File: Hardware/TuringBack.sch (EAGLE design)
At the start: 43 parts, among them IC11 78L09, IC12 78L09, IC7 TL072P

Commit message: Rev 4 Front and Back Boards complete
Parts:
- renumbered BACK_BUS2 to LINK1, BACK_PWR to LINK2, BUS_1_BACK to LINK3
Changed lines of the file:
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@@
 <part name="L1" library="inductors" deviceset="BL0" device="1RN1A"/>
 <part name="L2" library="inductors" deviceset="BL0" device="1RN1A"/>
-<part name="BACK_PWR" library="con-lstb" deviceset="MA03-2" device=""/>
+<part name="LINK2" library="con-lstb" deviceset="MA03-2" device=""/>
 <part name="R4" library="TomW" deviceset="R-EU_" device="0207/7" value="100k"/>
 <part name="C19" library="TomW" deviceset="C-EU" device="050-024X044" value="100n"/>
@@
 <part name="C24" library="TomW" deviceset="C-EU" device="050-024X044" value="100n"/>
 <part name="C25" library="TomW" deviceset="C-EU" device="050-024X044" value="100n"/>
-<part name="BACK_BUS2" library="con-lstb" deviceset="MA03-2" device=""/>
-<part name="BUS_1_BACK" library="con-lstb" deviceset="MA05-2" device=""/>
+<part name="LINK1" library="con-lstb" deviceset="MA03-2" device=""/>
+<part name="LINK3" library="con-lstb" deviceset="MA05-2" device=""/>
 </parts>
 <sheets>
@@
 <instance part="GATES" gate="G$1" x="43.18" y="50.8"/>
 <instance part="PULSES" gate="G$1" x="93.98" y="50.8"/>
-<instance part="BACK_PWR" gate="1" x="157.48" y="35.56"/>
-<instance part="BACK_BUS2" gate="1" x="157.48" y="20.32"/>
-<instance part="BUS_1_BACK" gate="G$1" x="157.48" y="53.34"/>
+<instance part="LINK2" gate="1" x="157.48" y="35.56"/>
+<instance part="LINK1" gate="1" x="157.48" y="20.32"/>
+<instance part="LINK3" gate="G$1" x="157.48" y="53.34"/>
 <instance part="AND_2" gate="C" x="215.9" y="109.22"/>
 <instance part="AND_2" gate="D" x="218.44" y="86.36"/>
@@
 </segment>
 <segment>
-<pinref part="BACK_BUS2" gate="1" pin="5"/>
+<pinref part="LINK1" gate="1" pin="5"/>
 <wire x1="167.64" y1="22.86" x2="165.1" y2="22.86" width="0.1524" layer="91"/>
 <label x="167.64" y="22.86" size="1.016" layer="95" xref="yes"/>
@@
 </segment>
 <segment>
-<pinref part="BACK_BUS2" gate="1" pin="6"/>
+<pinref part="LINK1" gate="1" pin="6"/>
 <wire x1="147.32" y1="22.86" x2="149.86" y2="22.86" width="0.1524" layer="91"/>
 <label x="147.32" y="22.86" size="1.016" layer="95" rot="R180" xref="yes"/>
@@
 </segment>
 <segment>
-<pinref part="BACK_PWR" gate="1" pin="6"/>
+<pinref part="LINK2" gate="1" pin="6"/>
 <wire x1="147.32" y1="38.1" x2="149.86" y2="38.1" width="0.1524" layer="91"/>
 <label x="147.32" y="38.1" size="1.016" layer="95" rot="R180" xref="yes"/>
 </segment>
 <segment>
-<pinref part="BACK_PWR" gate="1" pin="5"/>
+<pinref part="LINK2" gate="1" pin="5"/>
 <wire x1="167.64" y1="38.1" x2="165.1" y2="38.1" width="0.1524" layer="91"/>
 <label x="167.64" y="38.1" size="1.016" layer="95" xref="yes"/>
@@
 </segment>
 <segment>
-<pinref part="BACK_PWR" gate="1" pin="4"/>
+<pinref part="LINK2" gate="1" pin="4"/>
 <wire x1="147.32" y1="35.56" x2="149.86" y2="35.56" width="0.1524" layer="91"/>
 <label x="147.32" y="35.56" size="1.016" layer="95" rot="R180" xref="yes"/>
 </segment>
 <segment>
-<pinref part="BACK_PWR" gate="1" pin="3"/>
+<pinref part="LINK2" gate="1" pin="3"/>
 <wire x1="167.64" y1="35.56" x2="165.1" y2="35.56" width="0.1524" layer="91"/>
 <label x="167.64" y="35.56" size="1.016" layer="95" xref="yes"/>
@@
 </segment>
 <segment>
-<pinref part="BACK_BUS2" gate="1" pin="4"/>
+<pinref part="LINK1" gate="1" pin="4"/>
 <wire x1="147.32" y1="20.32" x2="149.86" y2="20.32" width="0.1524" layer="91"/>
 <label x="147.32" y="20.32" size="1.016" layer="95" rot="R180" xref="yes"/>
@@
 <wire x1="167.64" y1="58.42" x2="165.1" y2="58.42" width="0.1524" layer="91"/>
 <label x="167.64" y="58.42" size="1.016" layer="95" xref="yes"/>
-<pinref part="BUS_1_BACK" gate="G$1" pin="9"/>
+<pinref part="LINK3" gate="G$1" pin="9"/>
 </segment>
 <segment>
@@
 </segment>
 <segment>
-<pinref part="BACK_BUS2" gate="1" pin="2"/>
+<pinref part="LINK1" gate="1" pin="2"/>
 <wire x1="147.32" y1="17.78" x2="149.86" y2="17.78" width="0.1524" layer="91"/>
 <label x="147.32" y="17.78" size="1.016" layer="95" rot="R180" xref="yes"/>
@@
 </segment>
 <segment>
-<pinref part="BACK_BUS2" gate="1" pin="3"/>
+<pinref part="LINK1" gate="1" pin="3"/>
 <wire x1="167.64" y1="20.32" x2="165.1" y2="20.32" width="0.1524" layer="91"/>
 <label x="167.64" y="20.32" size="1.016" layer="95" xref="yes"/>
@@
 <wire x1="167.64" y1="48.26" x2="165.1" y2="48.26" width="0.1524" layer="91"/>
 <label x="167.64" y="48.26" size="1.016" layer="95" xref="yes"/>
-<pinref part="BUS_1_BACK" gate="G$1" pin="1"/>
+<pinref part="LINK3" gate="G$1" pin="1"/>
 </segment>
 <segment>
@@
 <wire x1="147.32" y1="48.26" x2="149.86" y2="48.26" width="0.1524" layer="91"/>
 <label x="147.32" y="48.26" size="1.016" layer="95" rot="R180" xref="yes"/>
-<pinref part="BUS_1_BACK" gate="G$1" pin="2"/>
+<pinref part="LINK3" gate="G$1" pin="2"/>
 </segment>
 <segment>
@@
 <wire x1="167.64" y1="50.8" x2="165.1" y2="50.8" width="0.1524" layer="91"/>
 <label x="167.64" y="50.8" size="1.016" layer="95" xref="yes"/>
-<pinref part="BUS_1_BACK" gate="G$1" pin="3"/>
+<pinref part="LINK3" gate="G$1" pin="3"/>
 </segment>
 <segment>
@@
 <wire x1="147.32" y1="50.8" x2="149.86" y2="50.8" width="0.1524" layer="91"/>
 <label x="147.32" y="50.8" size="1.016" layer="95" rot="R180" xref="yes"/>
-<pinref part="BUS_1_BACK" gate="G$1" pin="4"/>
+<pinref part="LINK3" gate="G$1" pin="4"/>
 </segment>
 <segment>
@@
 <wire x1="167.64" y1="53.34" x2="165.1" y2="53.34" width="0.1524" layer="91"/>
 <label x="167.64" y="53.34" size="1.016" layer="95" xref="yes"/>
-<pinref part="BUS_1_BACK" gate="G$1" pin="5"/>
+<pinref part="LINK3" gate="G$1" pin="5"/>
 </segment>
 <segment>
@@
 <wire x1="147.32" y1="53.34" x2="149.86" y2="53.34" width="0.1524" layer="91"/>
 <label x="147.32" y="53.34" size="1.016" layer="95" rot="R180" xref="yes"/>
-<pinref part="BUS_1_BACK" gate="G$1" pin="6"/>
+<pinref part="LINK3" gate="G$1" pin="6"/>
 </segment>
 <segment>
@@
 <wire x1="167.64" y1="55.88" x2="165.1" y2="55.88" width="0.1524" layer="91"/>
 <label x="167.64" y="55.88" size="1.016" layer="95" xref="yes"/>
-<pinref part="BUS_1_BACK" gate="G$1" pin="7"/>
+<pinref part="LINK3" gate="G$1" pin="7"/>
 </segment>
 <segment>
@@
 <wire x1="147.32" y1="55.88" x2="149.86" y2="55.88" width="0.1524" layer="91"/>
 <label x="147.32" y="55.88" size="1.016" layer="95" rot="R180" xref="yes"/>
-<pinref part="BUS_1_BACK" gate="G$1" pin="8"/>
+<pinref part="LINK3" gate="G$1" pin="8"/>
 </segment>
 <segment>
@@
 </segment>
 <segment>
-<pinref part="BACK_BUS2" gate="1" pin="1"/>
+<pinref part="LINK1" gate="1" pin="1"/>
 <wire x1="167.64" y1="17.78" x2="165.1" y2="17.78" width="0.1524" layer="91"/>
 <label x="167.64" y="17.78" size="1.016" layer="95" xref="yes"/>
@@
 </segment>
 <segment>
-<pinref part="BACK_PWR" gate="1" pin="2"/>
+<pinref part="LINK2" gate="1" pin="2"/>
 <wire x1="147.32" y1="33.02" x2="149.86" y2="33.02" width="0.1524" layer="91"/>
 <label x="147.32" y="33.02" size="1.016" layer="95" rot="R180" xref="yes"/>
 </segment>
 <segment>
-<pinref part="BACK_PWR" gate="1" pin="1"/>
+<pinref part="LINK2" gate="1" pin="1"/>
 <wire x1="167.64" y1="33.02" x2="165.1" y2="33.02" width="0.1524" layer="91"/>
 <label x="167.64" y="33.02" size="1.016" layer="95" xref="yes"/>
@@
 <wire x1="147.32" y1="58.42" x2="149.86" y2="58.42" width="0.1524" layer="91"/>
 <label x="147.32" y="58.42" size="1.016" layer="95" rot="R180" xref="yes"/>
-<pinref part="BUS_1_BACK" gate="G$1" pin="10"/>
-</segment>
-<segment>
+<pinref part="LINK3" gate="G$1" pin="10"/>
+</segment>
+<segment>

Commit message: Silkscreen change on Back Board
Added + - symbols to fuses in power supply
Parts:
- +FUSE: value FUSE -> +FUSE
- -FUSE: value FUSE -> -FUSE
- renumbered F1 to +FUSE, F2 to -FUSE
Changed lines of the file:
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@@
 <part name="D5" library="diode" deviceset="1N4004" device="" value="1N4001"/>
 <part name="D6" library="diode" deviceset="1N4004" device="" value="1N4001"/>
-<part name="F1" library="TomW" deviceset="PTC_FUSE" device="POLY_FUSE" value="FUSE"/>
-<part name="F2" library="TomW" deviceset="PTC_FUSE" device="POLY_FUSE" value="FUSE"/>
+<part name="+FUSE" library="TomW" deviceset="PTC_FUSE" device="POLY_FUSE" value="+FUSE"/>
+<part name="-FUSE" library="TomW" deviceset="PTC_FUSE" device="POLY_FUSE" value="-FUSE"/>
 <part name="L1" library="inductors" deviceset="BL0" device="1RN1A"/>
 <part name="L2" library="inductors" deviceset="BL0" device="1RN1A"/>
@@
 <instance part="D5" gate="1" x="83.82" y="109.22" rot="R90"/>
 <instance part="D6" gate="1" x="83.82" y="96.52" rot="R90"/>
-<instance part="F1" gate="G$1" x="93.98" y="114.3"/>
-<instance part="F2" gate="G$1" x="93.98" y="91.44"/>
+<instance part="+FUSE" gate="G$1" x="93.98" y="114.3"/>
+<instance part="-FUSE" gate="G$1" x="93.98" y="91.44"/>
 <instance part="L1" gate="G$1" x="113.03" y="114.3"/>
 <instance part="L2" gate="G$1" x="113.03" y="91.44"/>
@@
 </segment>
 <segment>
-<pinref part="F1" gate="G$1" pin="P$1"/>
+<pinref part="+FUSE" gate="G$1" pin="P$1"/>
 <pinref part="D5" gate="1" pin="C"/>
 <wire x1="88.9" y1="114.3" x2="83.82" y2="114.3" width="0.1524" layer="91"/>
@@
 </segment>
 <segment>
-<pinref part="F2" gate="G$1" pin="P$1"/>
+<pinref part="-FUSE" gate="G$1" pin="P$1"/>
 <wire x1="73.66" y1="91.44" x2="83.82" y2="91.44" width="0.1524" layer="91"/>
 <label x="73.66" y="91.44" size="1.778" layer="95" rot="R180" xref="yes"/>
@@
 <segment>
 <pinref part="L1" gate="G$1" pin="1"/>
-<pinref part="F1" gate="G$1" pin="P$2"/>
+<pinref part="+FUSE" gate="G$1" pin="P$2"/>
 <wire x1="107.95" y1="114.3" x2="99.06" y2="114.3" width="0.1524" layer="91"/>
 </segment>
@@
 <net name="N$44" class="1">
 <segment>
-<pinref part="F2" gate="G$1" pin="P$2"/>
+<pinref part="-FUSE" gate="G$1" pin="P$2"/>
 <pinref part="L2" gate="G$1" pin="1"/>
 <wire x1="107.95" y1="91.44" x2="99.06" y2="91.44" width="0.1524" layer="91"/>

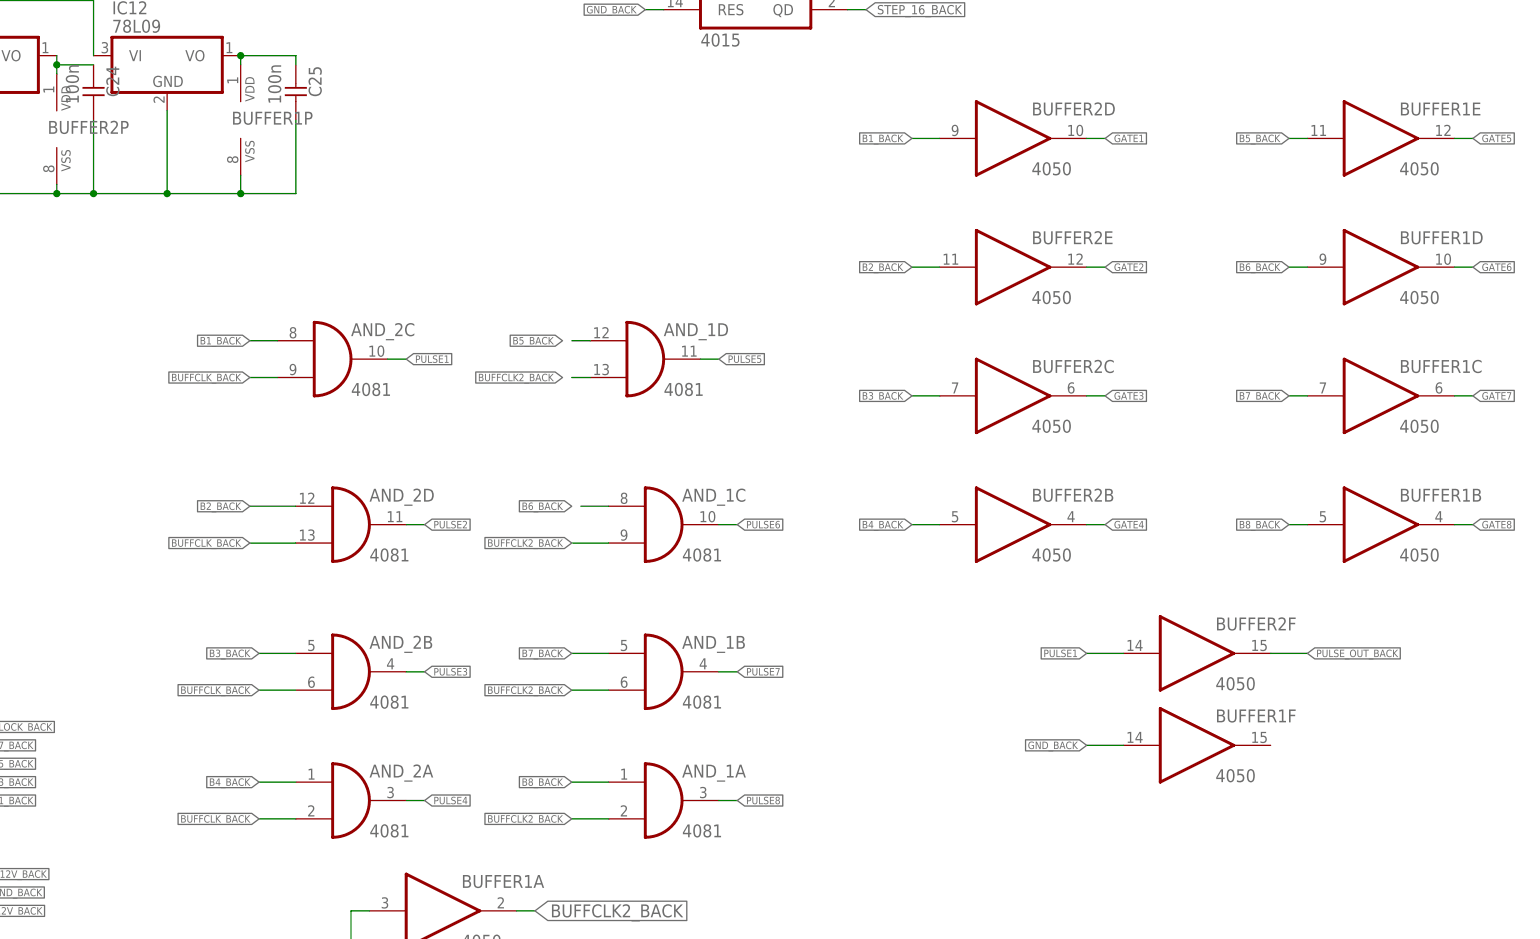
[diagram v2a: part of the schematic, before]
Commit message: Schematic fixed, back board needs to be routed
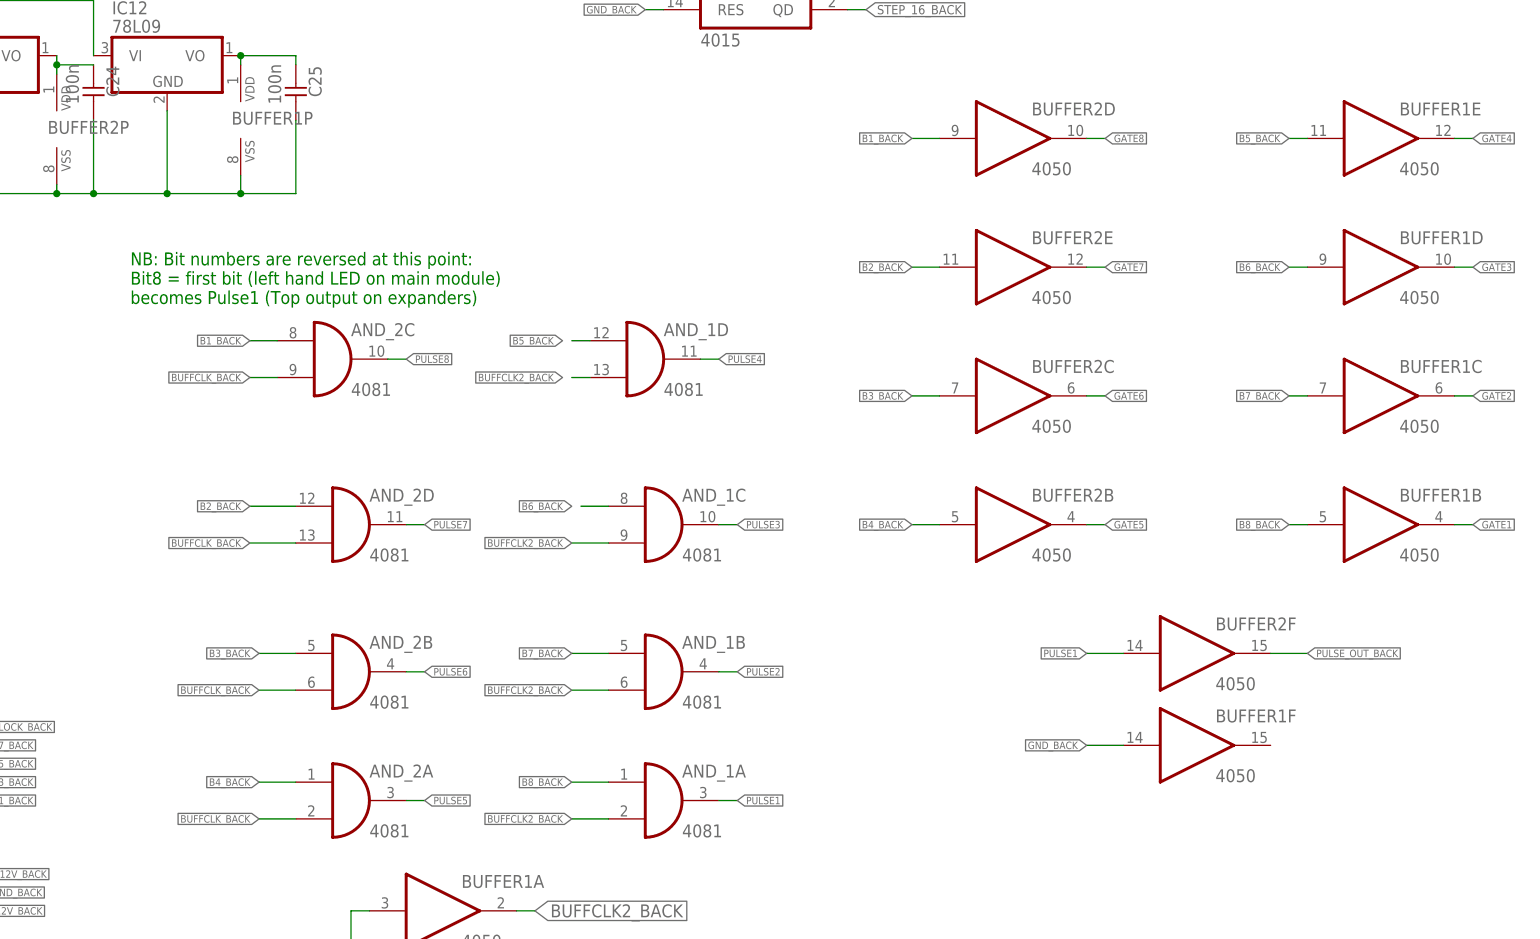
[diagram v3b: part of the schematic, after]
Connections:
- net GATE1: now also BUFFER1B.O; no longer BUFFER2D.O
- net GATE2: now also BUFFER1C.O; no longer BUFFER2E.O
- net GATE3: now also BUFFER1D.O; no longer BUFFER2C.O
- net GATE4: now also BUFFER1E.O; no longer BUFFER2B.O
- net GATE5: now also BUFFER2B.O; no longer BUFFER1E.O
- net GATE6: now also BUFFER2C.O; no longer BUFFER1D.O
- net GATE7: now also BUFFER2E.O; no longer BUFFER1C.O
- net GATE8: now also BUFFER2D.O; no longer BUFFER1B.O
- net PULSE1: now also AND_1A.O; no longer AND_2C.O
- net PULSE2: now also AND_1B.O; no longer AND_2D.O
- net PULSE3: now also AND_1C.O; no longer AND_2B.O
- net PULSE4: now also AND_1D.O; no longer AND_2A.O
- net PULSE5: now also AND_2A.O; no longer AND_1D.O
- net PULSE6: now also AND_2B.O; no longer AND_1C.O
- net PULSE7: now also AND_2D.O; no longer AND_1B.O
- net PULSE8: now also AND_2C.O; no longer AND_1A.O
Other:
- note added: "NB: Bit numbers are reversed at this point: Bit8 = first bit (left hand LED on main module) becomes Pulse1 (Top output on expanders)"

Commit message: First fully routed
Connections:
- net B1_BACK: now also AND_2A.I0; no longer AND_2C.I0
- net B4_BACK: now also AND_2C.I0; no longer AND_2A.I0
- net PULSE5: now also AND_2C.O; no longer AND_2A.O
- net PULSE8: now also AND_2A.O; no longer AND_2C.O
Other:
- moved on the sheet: AND_2A, AND_2C
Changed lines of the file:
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@@
 <?xml version="1.0" encoding="utf-8"?>
 <!DOCTYPE eagle SYSTEM "eagle.dtd">
-<eagle version="7.2.0">
+<eagle version="7.4.0">
 <drawing>
 <settings>
@@
 <instance part="LINK1" gate="1" x="157.48" y="20.32"/>
 <instance part="LINK3" gate="G$1" x="157.48" y="53.34"/>
-<instance part="AND_2" gate="C" x="215.9" y="109.22"/>
+<instance part="AND_2" gate="A" x="215.9" y="109.22"/>
 <instance part="AND_2" gate="D" x="218.44" y="86.36"/>
 <instance part="AND_2" gate="B" x="218.44" y="66.04"/>
-<instance part="AND_2" gate="A" x="218.44" y="48.26"/>
+<instance part="AND_2" gate="C" x="218.44" y="48.26"/>
 <instance part="AND_1" gate="D" x="259.08" y="109.22"/>
 <instance part="AND_1" gate="C" x="261.62" y="86.36"/>
@@
 </segment>
 <segment>
-<pinref part="AND_2" gate="C" pin="I0"/>
+<pinref part="AND_2" gate="A" pin="I0"/>
 <wire x1="204.47" y1="111.76" x2="208.28" y2="111.76" width="0.1524" layer="91"/>
 <label x="204.47" y="111.76" size="1.016" layer="95" rot="R180" xref="yes"/>
@@
 </segment>
 <segment>
-<pinref part="AND_2" gate="A" pin="I0"/>
+<pinref part="AND_2" gate="C" pin="I0"/>
 <wire x1="205.74" y1="50.8" x2="210.82" y2="50.8" width="0.1524" layer="91"/>
 <label x="205.74" y="50.8" size="1.016" layer="95" rot="R180" xref="yes"/>
@@
 </segment>
 <segment>
-<pinref part="AND_2" gate="C" pin="I1"/>
+<pinref part="AND_2" gate="A" pin="I1"/>
 <wire x1="204.47" y1="106.68" x2="208.28" y2="106.68" width="0.1524" layer="91"/>
 <label x="204.47" y="106.68" size="1.016" layer="95" rot="R180" xref="yes"/>
@@
 </segment>
 <segment>
-<pinref part="AND_2" gate="A" pin="I1"/>
+<pinref part="AND_2" gate="C" pin="I1"/>
 <wire x1="205.74" y1="45.72" x2="210.82" y2="45.72" width="0.1524" layer="91"/>
 <label x="205.74" y="45.72" size="1.016" layer="95" rot="R180" xref="yes"/>
@@
 </segment>
 <segment>
-<pinref part="AND_2" gate="A" pin="O"/>
+<pinref part="AND_2" gate="C" pin="O"/>
 <wire x1="228.6" y1="48.26" x2="226.06" y2="48.26" width="0.1524" layer="91"/>
 <label x="228.6" y="48.26" size="1.016" layer="95" xref="yes"/>
@@
 </segment>
 <segment>
-<pinref part="AND_2" gate="C" pin="O"/>
+<pinref part="AND_2" gate="A" pin="O"/>
 <wire x1="226.06" y1="109.22" x2="223.52" y2="109.22" width="0.1524" layer="91"/>
 <label x="226.06" y="109.22" size="1.016" layer="95" xref="yes"/>

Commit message: Finished routing + gerber uploaded
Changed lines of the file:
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@@
+Bit8 = first bit (left hand LED on main module)
+becomes Pulse1 (Top output on expanders) </text>
+<text x="312.42" y="152.4" size="1.778" layer="91">NB: Bit numbers are reversed at this point:
 Bit8 = first bit (left hand LED on main module)
 becomes Pulse1 (Top output on expanders) </text>
